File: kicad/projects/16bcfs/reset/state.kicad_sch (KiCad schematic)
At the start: 13 parts, among them U10 74HC123, U11 74HC03, U5 74HC00, U8 74HC00, U9 74HC02

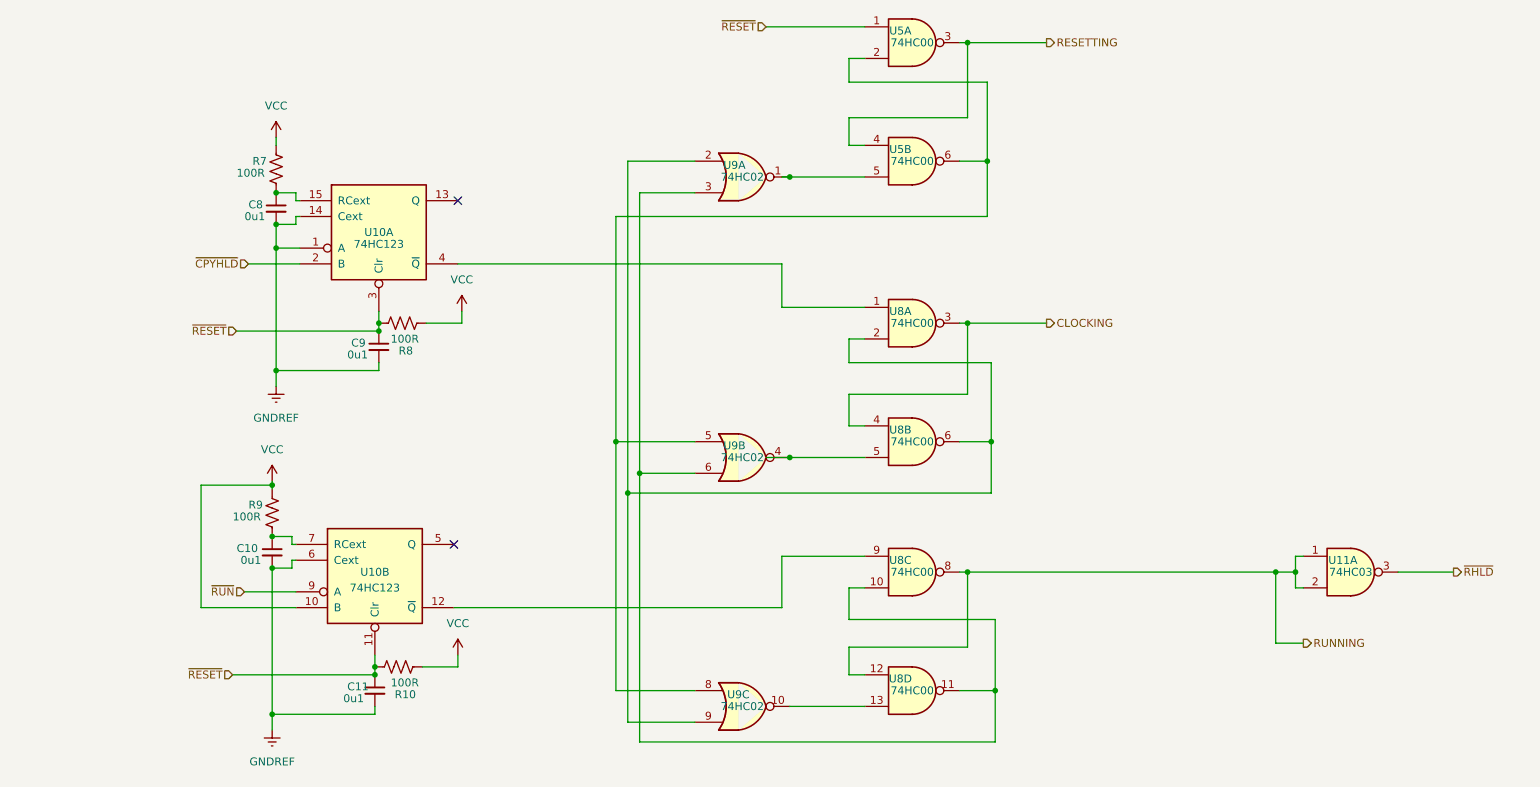
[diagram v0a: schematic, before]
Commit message: Added some debugging code
This is still not working.  I will need to revamp the reset routines for
the emulator to get this to work properly.  Everything will need an
initial state on construction and a `reset()` routine to place
everything into a proper state.  This in itself will be a major change.
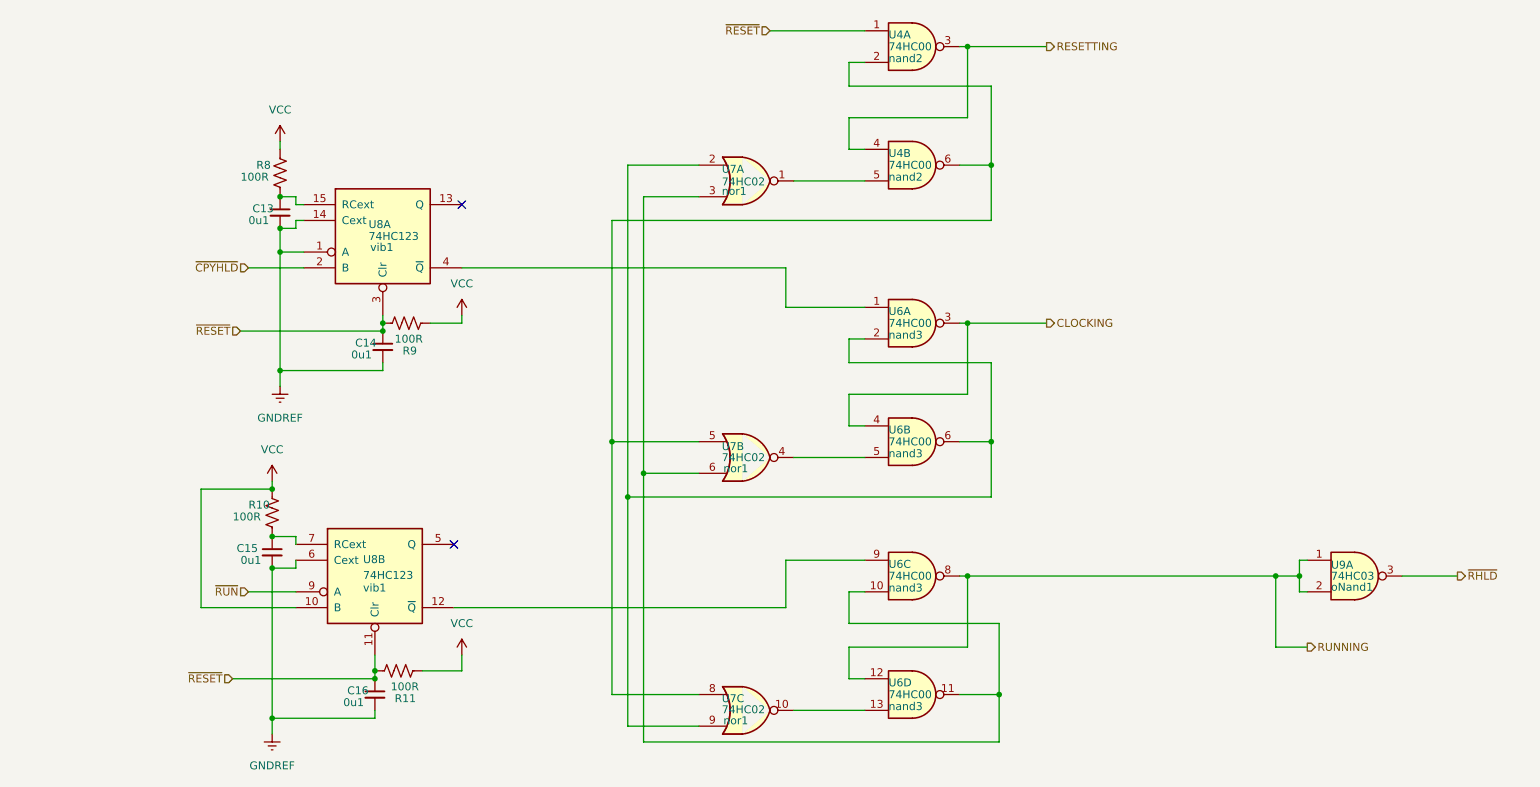
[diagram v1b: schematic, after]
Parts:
- U4: renamed from U5; name (none) -> nand2
- U6: renamed from U8; name (none) -> nand3
- U7: renamed from U9; name (none) -> nor1
- U8: renamed from U10; name (none) -> vib1
- U9: renamed from U11; name (none) -> oNand1
- renumbered C8 to C13, C9 to C14, C10 to C15, C11 to C16, R9 to R10, R10 to R11, R7 to R8, R8 to R9
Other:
- moved on the sheet: C13, C14, C16, R11, R8, R9, U4A, U4B, U6C, U6D, U7A, U7B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

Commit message: Make a number of changes to the schematic and emulator
These changes are incremental to getting the emulator to work, they are
needed for making sure that the RESETTING, CLOCKING, and RUNNING signals
are processed properly.

There is also quite a bit of debugging code which gets added/removed
ahead of this commit.
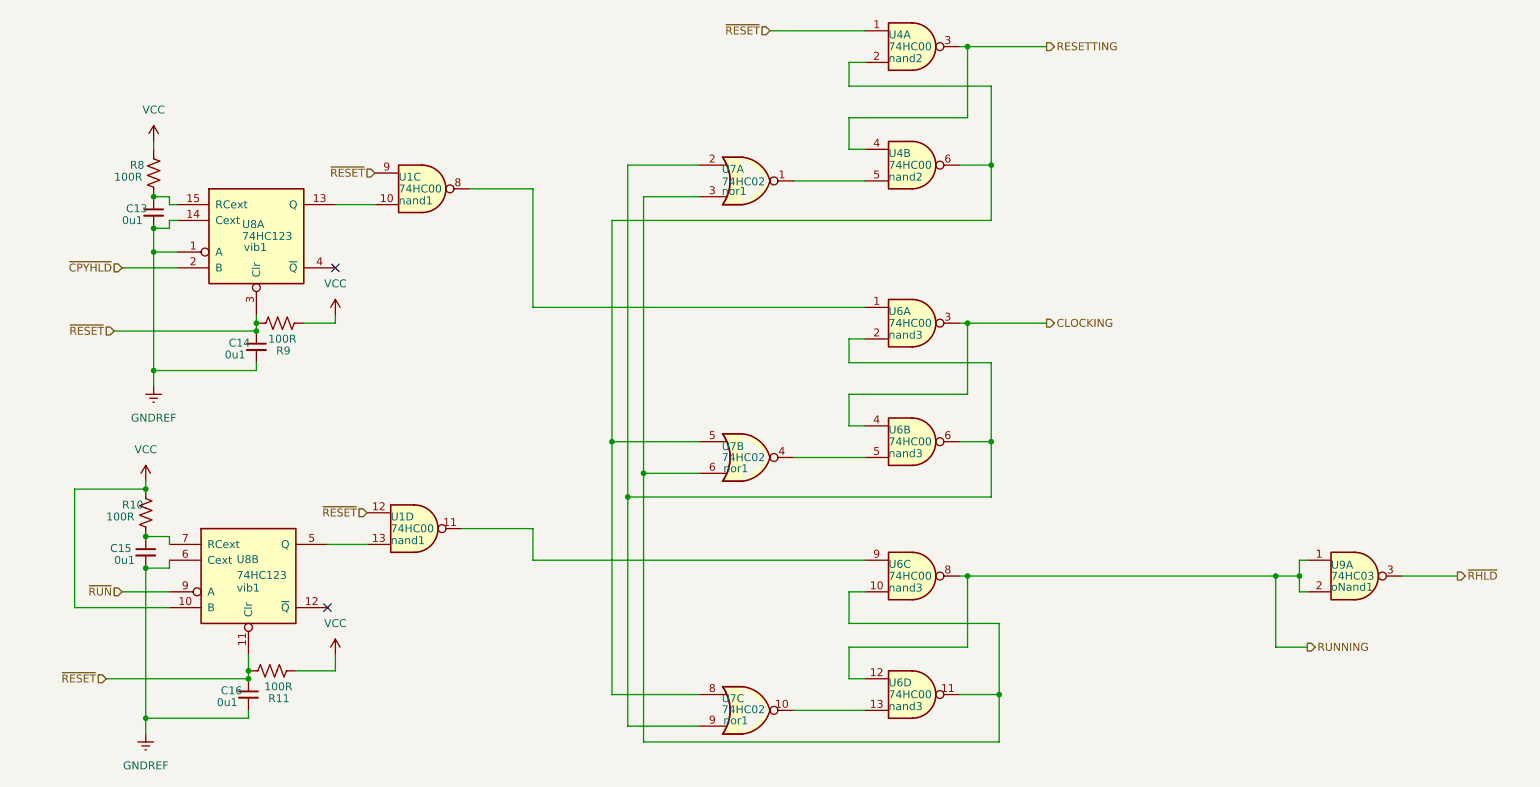
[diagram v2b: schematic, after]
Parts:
- added U1: 74HC00, symbol 74xx:74HC00
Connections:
- net ~{RESET}: now also U1.12, U1.9
- net at U8.13 (Q): now also U1.10
- net at U8.4 (~{Q}): no longer U6.1
- net at U6.9: now also U1.11; no longer U8.12 (~{Q})
- net at U8.5 (Q): now also U1.13
- new net: U1.8, U6.1
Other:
- moved on the sheet: C13, C14, C15, C16, R10, R11, R8, R9, U8A, U8B

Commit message: Make the final changes needed to get the Reset Circuit working
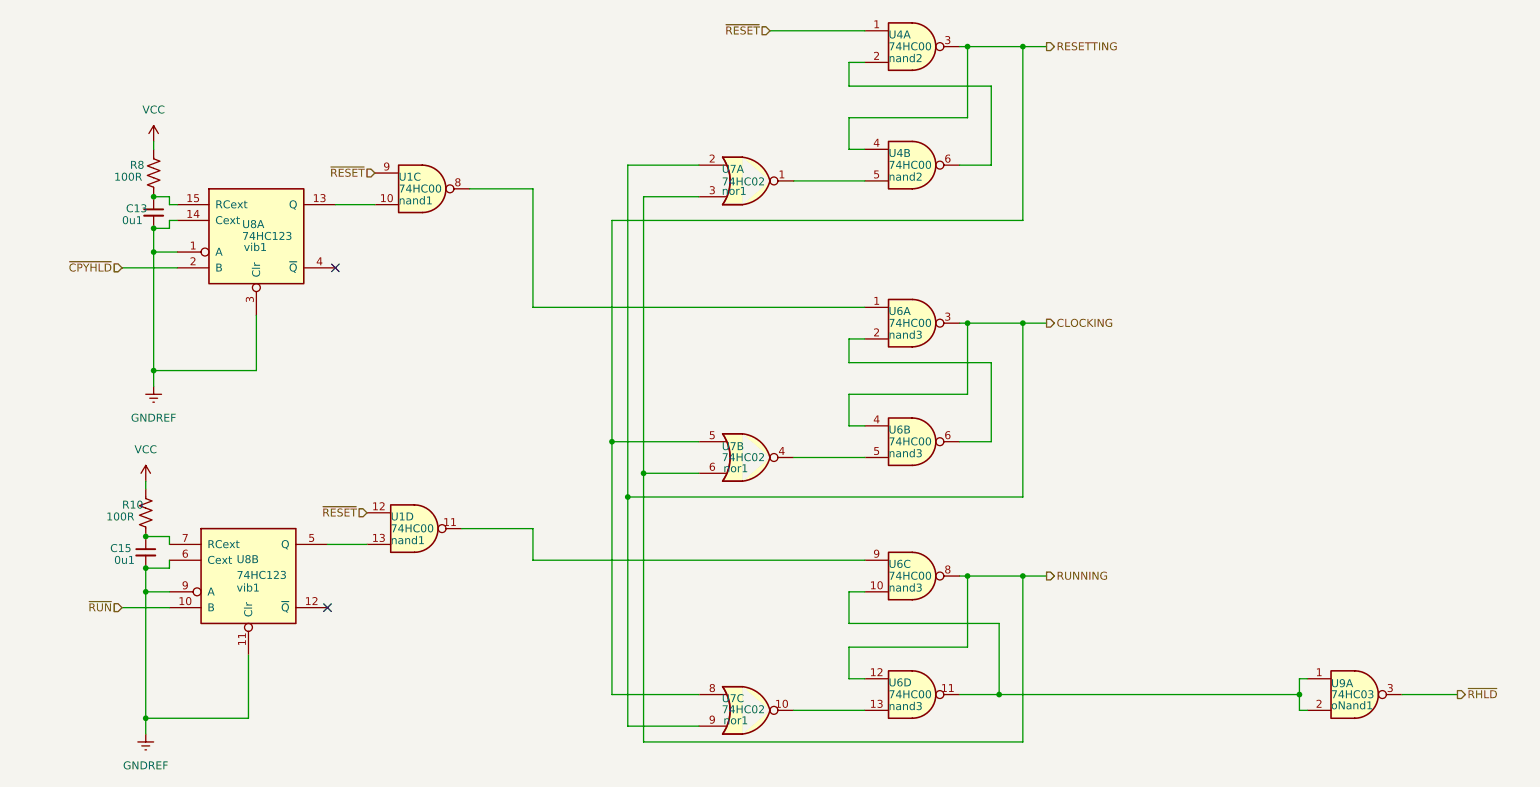
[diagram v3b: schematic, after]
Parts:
- removed C14, C16: 0u1, symbol Device:C_Small
- removed R11, R9: 100R, symbol Device:R_US
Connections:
- net CLOCKING: now also U7.2, U7.9
- net GNDREF: now also U8.11 (Clr), U8.3 (Clr), U8.9 (A)
- net RESETTING: now also U7.5, U7.8
- net RUNNING: now also U7.3, U7.6; no longer U9.1, U9.2
- net VCC: no longer U8.10 (B)
- net ~{RESET}: no longer U8.11 (Clr), U8.3 (Clr)
- net ~{RUN}: now also U8.10 (B); no longer U8.9 (A)
- net at U4.2, U4.6: no longer U7.5, U7.8
- net at U6.2, U6.6: no longer U7.2, U7.9
- net at U6.10, U6.11: now also U9.1, U9.2; no longer U7.3, U7.6
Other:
- moved on the sheet: U9A

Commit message: Correct a save issue with KiCad
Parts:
- removed U1: 74HC00, symbol 74xx:74HC00
- added unit 3 of U4
- added unit 4 of U4
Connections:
- net ~{RESET}: now also U4.12, U4.9
- net at U8.13 (Q): now also U4.10
- net at U6.1: now also U4.8
- net at U6.9: now also U4.11
- net at U8.5 (Q): now also U4.13
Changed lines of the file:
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@@
+    )
+  )
+  (symbol (lib_id "74xx:74HC00") (at 76.2 60.96 0) (unit 3)
+    (in_bom yes) (on_board yes) (dnp no)
+    (property "Reference" "U4" (at 72.39 58.42 0)
+      (effects (font (size 1.27 1.27)) (justify left))
+    )
+    (property "Value" "74HC00" (at 72.39 60.96 0)
+      (effects (font (size 1.27 1.27)) (justify left))
+    )
+    (property "Footprint" "" (at 76.2 60.96 0)
+      (effects (font (size 1.27 1.27)) hide)
+    )
+    (property "Datasheet" "http://www.ti.com/lit/gpn/sn74hc00" (at 76.2 60.96 0)
+      (effects (font (size 1.27 1.27)) hide)
+    )
+    (property "name" "nand2" (at 72.39 62.865 0)
+      (effects (font (size 1.27 1.27)) (justify left))
+    )
+    (pin "7")
+    (pin "10")
+    (pin "4")
+    (pin "2")
+    (pin "14")
+    (pin "1")
+    (pin "3")
+    (pin "13")
+    (pin "11")
+    (pin "6")
+    (pin "9")
+    (pin "12")
+    (pin "5")
+    (pin "8")
+    (instances
+      (project "reset"
+        (path "/d0ae44e5-d74e-4df6-bf3d-e0535c5a7785/06c29919-d2e5-4aee-8c7c-b5e0134cf05f"
+          (reference "U4") (unit 3)
+        )
+      )
     )
   )
@@
     )
   )
-  (symbol (lib_id "74xx:74HC00") (at 74.93 115.57 0) (unit 4)
-    (in_bom yes) (on_board yes) (dnp no)
-    (property "Reference" "U1" (at 71.12 113.665 0)
-      (effects (font (size 1.27 1.27)) (justify left))
-    )
-    (property "Value" "74HC00" (at 71.12 115.57 0)
-      (effects (font (size 1.27 1.27)) (justify left))
-    )
-    (property "Footprint" "" (at 74.93 115.57 0)
-      (effects (font (size 1.27 1.27)) hide)
-    )
-    (property "Datasheet" "http://www.ti.com/lit/gpn/sn74hc00" (at 74.93 115.57 0)
-      (effects (font (size 1.27 1.27)) hide)
-    )
-    (property "name" "nand1" (at 71.12 117.475 0)
-      (effects (font (size 1.27 1.27)) (justify left))
-    )
-    (pin "14")
-    (pin "7")
-    (pin "13")
-    (pin "10")
-    (pin "6")
-    (pin "12")
-    (pin "9")
-    (pin "2")
-    (pin "3")
-    (pin "1")
-    (pin "4")
-    (pin "5")
-    (pin "11")
-    (pin "8")
-    (instances
-      (project "reset"
-        (path "/d0ae44e5-d74e-4df6-bf3d-e0535c5a7785/06c29919-d2e5-4aee-8c7c-b5e0134cf05f"
-          (reference "U1") (unit 4)
-        )
-      )
-    )
-  )
   (symbol (lib_id "eryjus:74HC03") (at 226.06 142.24 0) (unit 1)
     (in_bom yes) (on_board yes) (dnp no)
@@
     )
   )
-  (symbol (lib_id "74xx:74HC00") (at 76.2 60.96 0) (unit 3)
-    (in_bom yes) (on_board yes) (dnp no)
-    (property "Reference" "U1" (at 72.39 59.055 0)
-      (effects (font (size 1.27 1.27)) (justify left))
-    )
-    (property "Value" "74HC00" (at 72.39 60.96 0)
-      (effects (font (size 1.27 1.27)) (justify left))
-    )
-    (property "Footprint" "" (at 76.2 60.96 0)
-      (effects (font (size 1.27 1.27)) hide)
-    )
-    (property "Datasheet" "http://www.ti.com/lit/gpn/sn74hc00" (at 76.2 60.96 0)
-      (effects (font (size 1.27 1.27)) hide)
-    )
-    (property "name" "nand1" (at 72.39 62.865 0)
-      (effects (font (size 1.27 1.27)) (justify left))
-    )
-    (pin "14")
-    (pin "7")
-    (pin "13")
-    (pin "10")
-    (pin "6")
-    (pin "12")
-    (pin "9")
-    (pin "2")
-    (pin "3")
-    (pin "1")
-    (pin "4")
-    (pin "5")
-    (pin "11")
-    (pin "8")
-    (instances
-      (project "reset"
-        (path "/d0ae44e5-d74e-4df6-bf3d-e0535c5a7785/06c29919-d2e5-4aee-8c7c-b5e0134cf05f"
-          (reference "U1") (unit 3)
-        )
-      )
-    )
-  )
   (symbol (lib_id "Device:R_US") (at 33.02 58.42 0) (unit 1)
     (in_bom yes) (on_board yes) (dnp no)
@@
         )
       )
+    )
+  )
+  (symbol (lib_id "74xx:74HC00") (at 74.93 115.57 0) (unit 4)
+    (in_bom yes) (on_board yes) (dnp no)
+    (property "Reference" "U4" (at 71.12 113.03 0)
+      (effects (font (size 1.27 1.27)) (justify left))
+    )
+    (property "Value" "74HC00" (at 71.12 115.57 0)
+      (effects (font (size 1.27 1.27)) (justify left))
+    )
+    (property "Footprint" "" (at 74.93 115.57 0)
+      (effects (font (size 1.27 1.27)) hide)
+    )
+    (property "Datasheet" "http://www.ti.com/lit/gpn/sn74hc00" (at 74.93 115.57 0)
+      (effects (font (size 1.27 1.27)) hide)
+    )
+    (property "name" "nand2" (at 71.12 117.475 0)
+      (effects (font (size 1.27 1.27)) (justify left))
+    )
+    (pin "7")
+    (pin "10")
+    (pin "4")
+    (pin "2")
+    (pin "14")
+    (pin "1")
+    (pin "3")
+    (pin "13")
+    (pin "11")
+    (pin "6")
+    (pin "9")
+    (pin "12")
+    (pin "5")
+    (pin "8")
+    (instances
+      (project "reset"
+        (path "/d0ae44e5-d74e-4df6-bf3d-e0535c5a7785/06c29919-d2e5-4aee-8c7c-b5e0134cf05f"
+          (reference "U4") (unit 4)
+        )
+      )
